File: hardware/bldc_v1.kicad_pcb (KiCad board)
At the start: 4 copper layers, 63 parts, among them J1 Conn_01x06, J2 1x2_ScrewTerminal_65A, J3 Screw_Terminal_01x05, J4 RJ45, J5 Screw_Terminal_01x03, M1 IPB044N15N5, M2 IPB044N15N5, M3 IPB044N15N5, M4 IPB044N15N5, M5 IPB044N15N5, M6 IPB044N15N5, M7 STM32F4-DISCOVERY, U1 AD8205, U2 AD8205

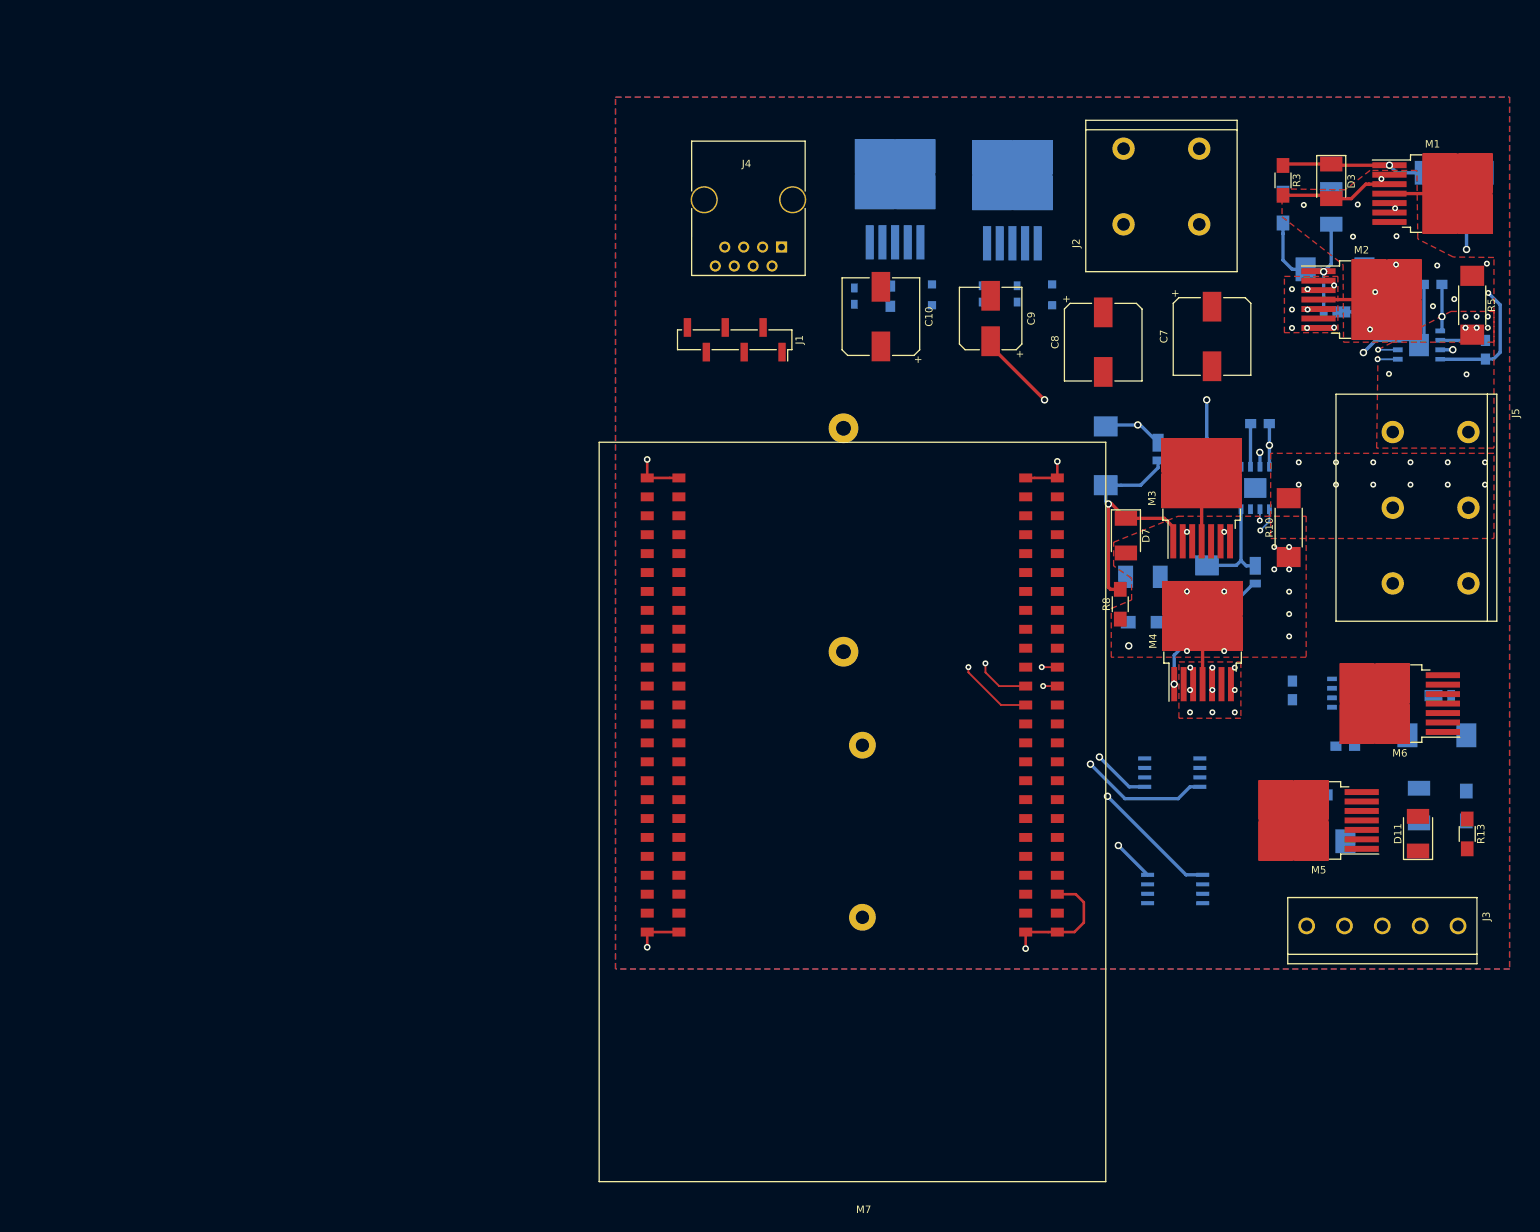
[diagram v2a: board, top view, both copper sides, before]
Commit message: Completed routing
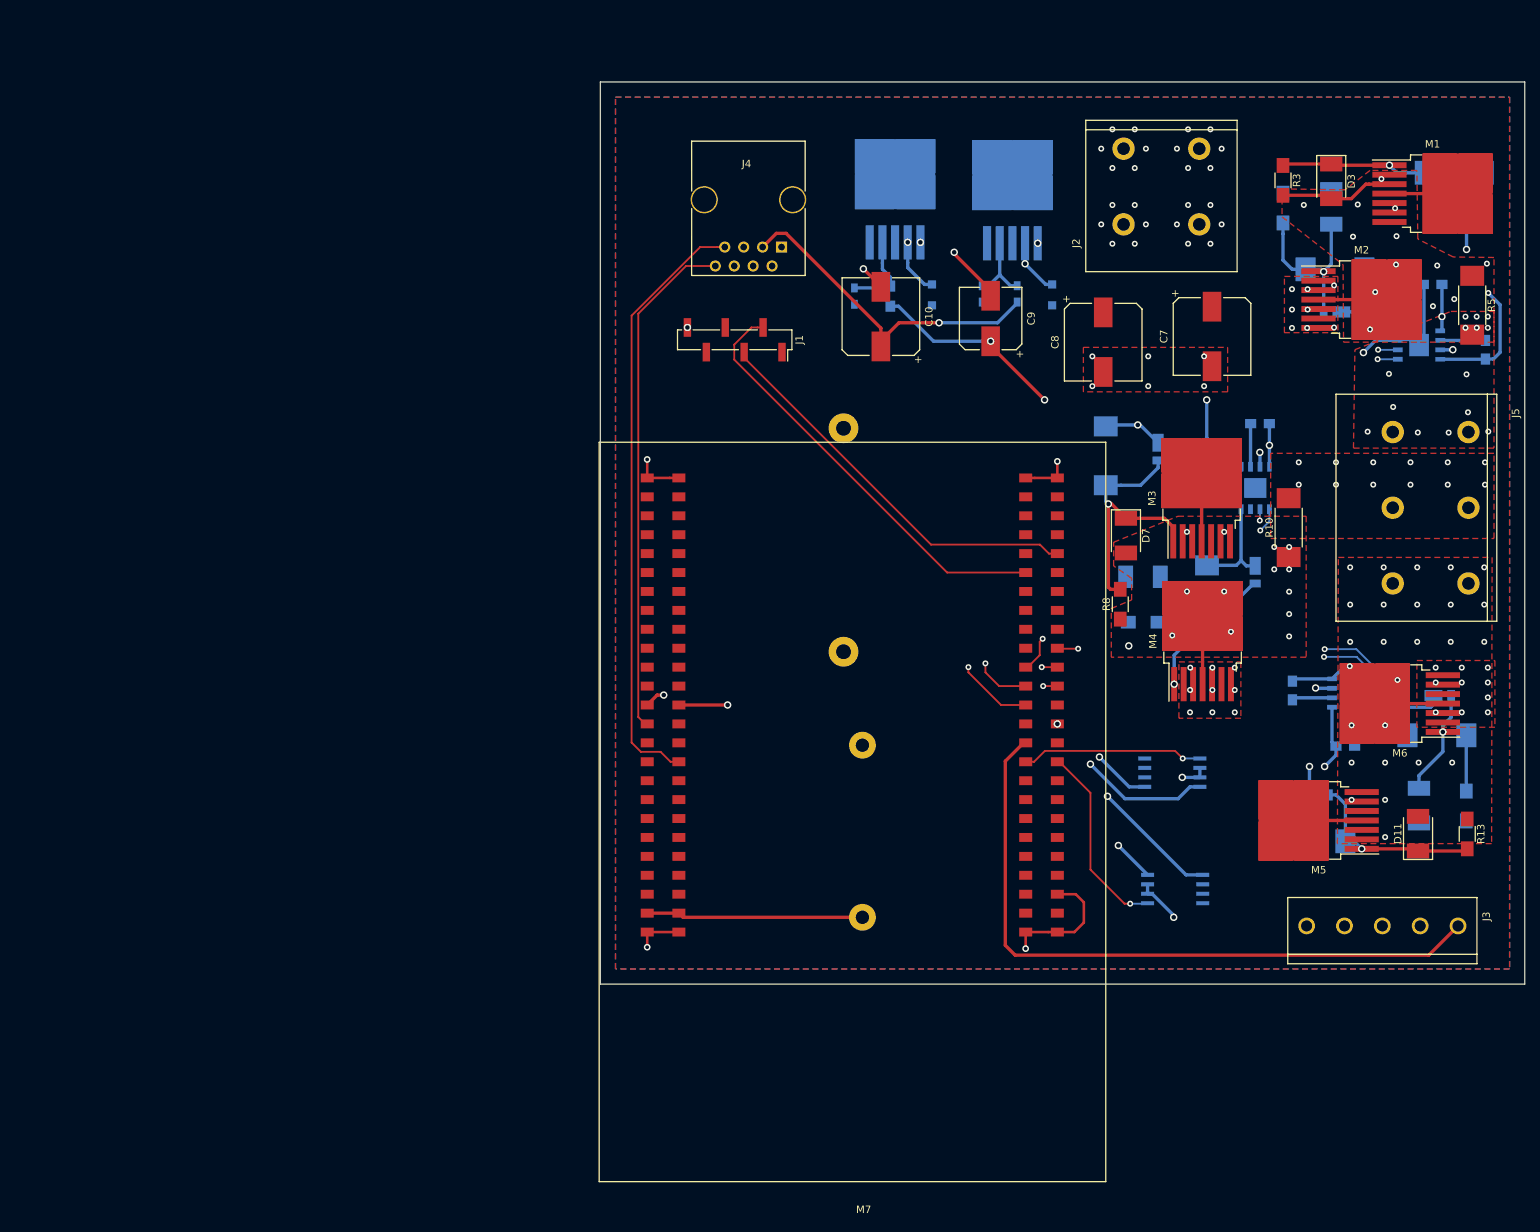
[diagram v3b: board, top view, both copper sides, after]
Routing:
- net /5v: track 0.00 -> 248.1 mm, vias 0 -> 3
- net /GateDriver/+12V: track 90.4 -> 236.9 mm, vias 3 -> 5
- net /Microcontroller/HALL_B: track 0.00 -> 118.4 mm, vias 0 -> 1
- net /Microcontroller/HALL_A: track 0.00 -> 108.0 mm, vias 0 -> 1
- net /Microcontroller/HALL_C: track 0.00 -> 91.4 mm
- net Net-(5vConverter1-Pad2): track 0.00 -> 87.1 mm, vias 0 -> 1
- net /Microcontroller/I2C_SCL: track 0.00 -> 81.0 mm
- net /Microcontroller/I2C_SDA: track 0.00 -> 68.7 mm
- net /Microcontroller/USART_TX: track 0.00 -> 57.8 mm
- net /GateDriver/LS_C_TTL_PWM: track 0.00 -> 55.6 mm, vias 0 -> 2
- net /Microcontroller/USART_RX: track 0.00 -> 53.7 mm
- net /GateDriver/HS_C_TTL_PWM: track 0.00 -> 44.6 mm, vias 0 -> 2
- net Net-(12vConverter1-Pad2): track 0.00 -> 36.1 mm, vias 0 -> 1
- net /FB_B: track 0.00 -> 26.1 mm, vias 0 -> 1
- net Net-(D10-Pad2): track 0.00 -> 25.1 mm, vias 0 -> 1
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- added copper zone on Inner2.Cu, net /48v
- added copper zone on Inner3.Cu, net /48v
- added copper zone on Inner2.Cu, net /GND
- added copper zone on Inner3.Cu, net /GND
- added copper zone on F.Cu, net /MOSFETS/PhaseC
- added copper zone on Inner2.Cu, net /MOSFETS/PhaseC
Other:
- board outline added: 124.1 x 121.1 mm

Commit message: Added additional planes for extra current
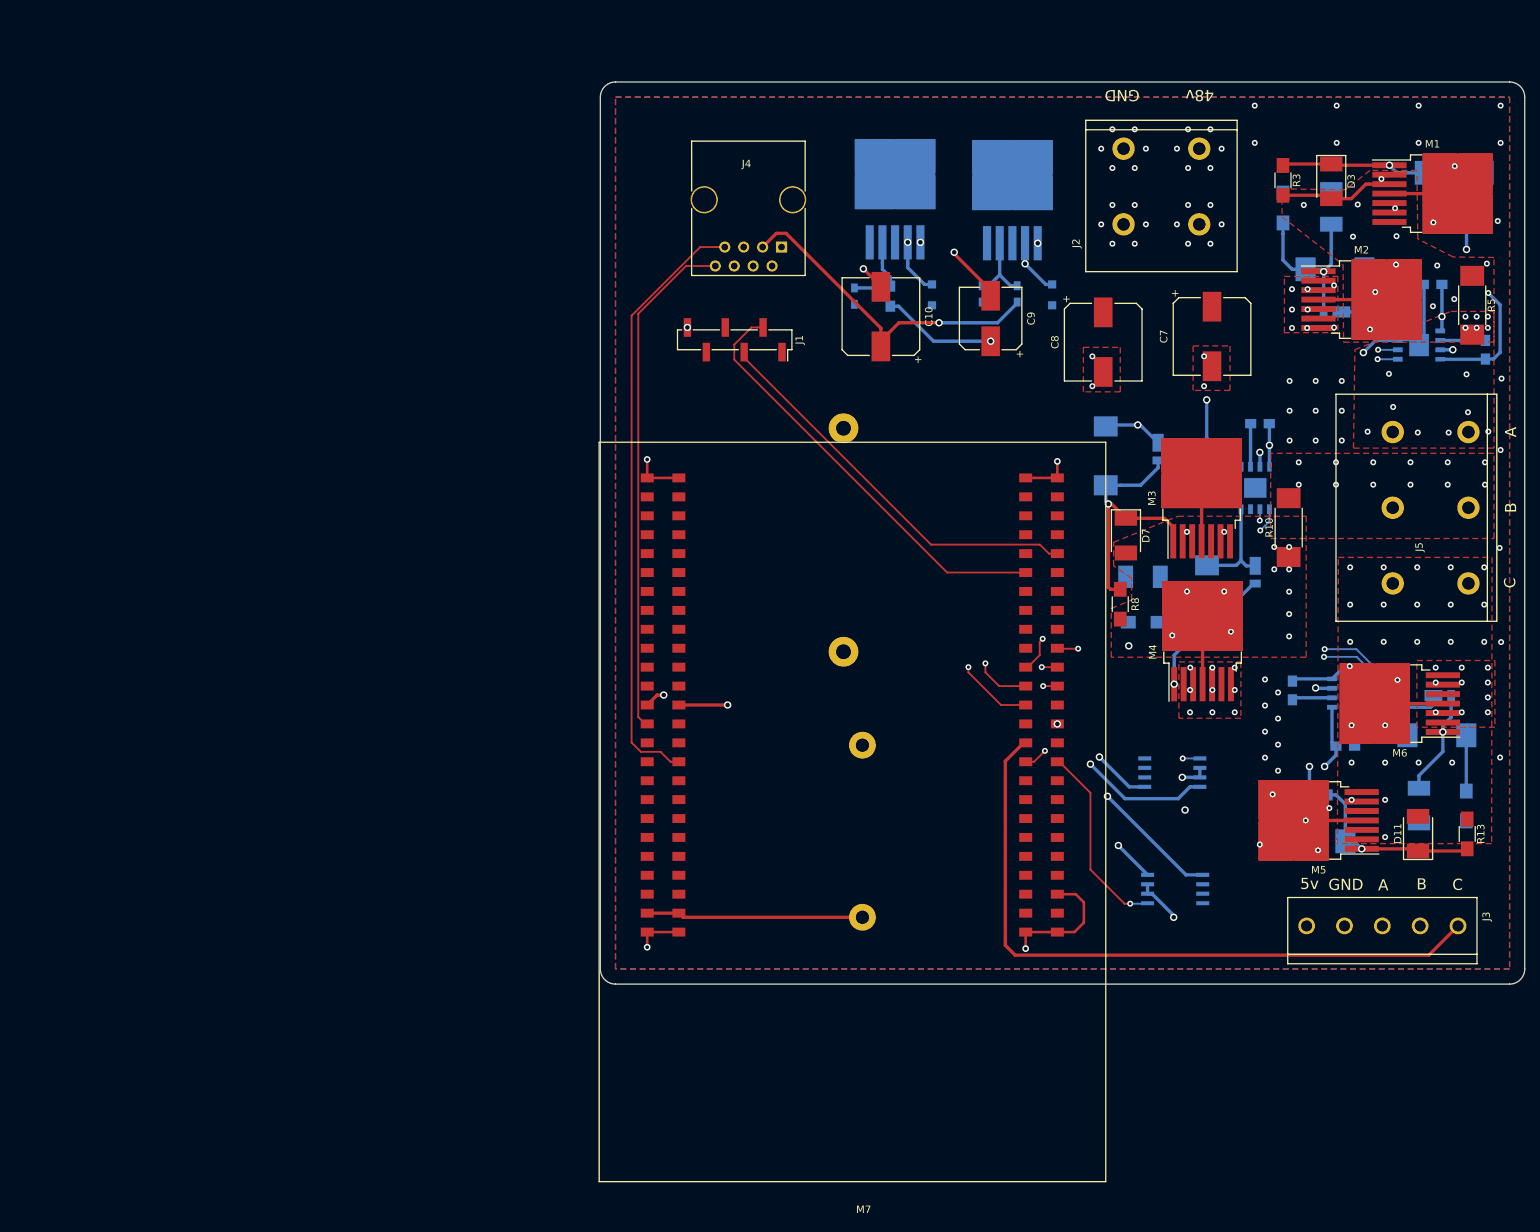
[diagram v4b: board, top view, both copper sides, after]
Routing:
- net /FB_A: vias 1 -> 2
- net /48v: vias 14 -> 50
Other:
- outline, holes or cut-outs redrawn
- board text added: "48v"
- board text added: "5v"
- board text added: "A"
- board text added: "B"
- board text added: "C"
- board text added: "GND"

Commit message: updated routing and all plots
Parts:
- moved 12vConverter1 36.4 mm to (117.5, 38.8)
- moved 5vConverter1 36.4 mm to (133.3, 38.9)
- moved C1 36.4 mm to (166.5, 68.9)
- moved C10 36.4 mm to (115.6, 54.5)
- moved C2 36.4 mm to (170.9, 104.7)
- moved C3 36.4 mm to (196.8, 59.0)
- moved C4 36.4 mm to (189.7, 50.2)
- moved C5 36.4 mm to (158.8, 75.7)
- moved C6 36.4 mm to (178.0, 112.2)
- moved C7 36.4 mm to (160.1, 57.2)
- moved C8 36.4 mm to (145.5, 58.0)
- moved C9 36.4 mm to (130.4, 54.8)
- moved D1 36.4 mm to (192.8, 40.1)
- moved D10 36.4 mm to (190.7, 105.4)
- moved D11 36.4 mm to (187.7, 124.0)
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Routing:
- net /48v: track 27.4 -> 82.2 mm
- net /GND: track 63.0 -> 106.9 mm, vias 54 -> 66
- net /GateDriver/PhaseASource: track 145.9 -> 130.7 mm
- net /GateDriver/+12V: track 236.7 -> 237.8 mm
- net /MOSFETS/PhaseC: vias 26 -> 27
- net /MOSFETS/PhaseB: vias 13 -> 17
- net /GateDriver/PhaseBSource: vias 16 -> 17

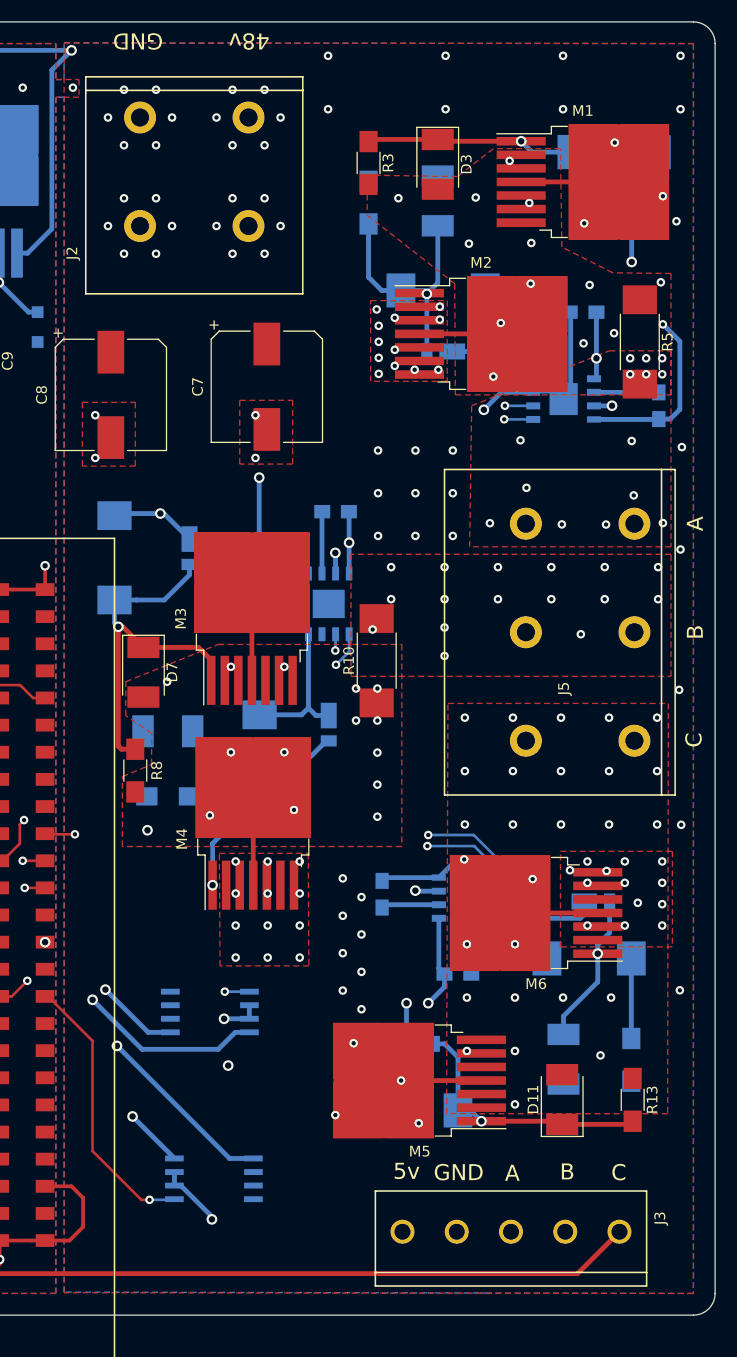
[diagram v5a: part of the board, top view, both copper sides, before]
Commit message: Updated schematic for additional capacitors
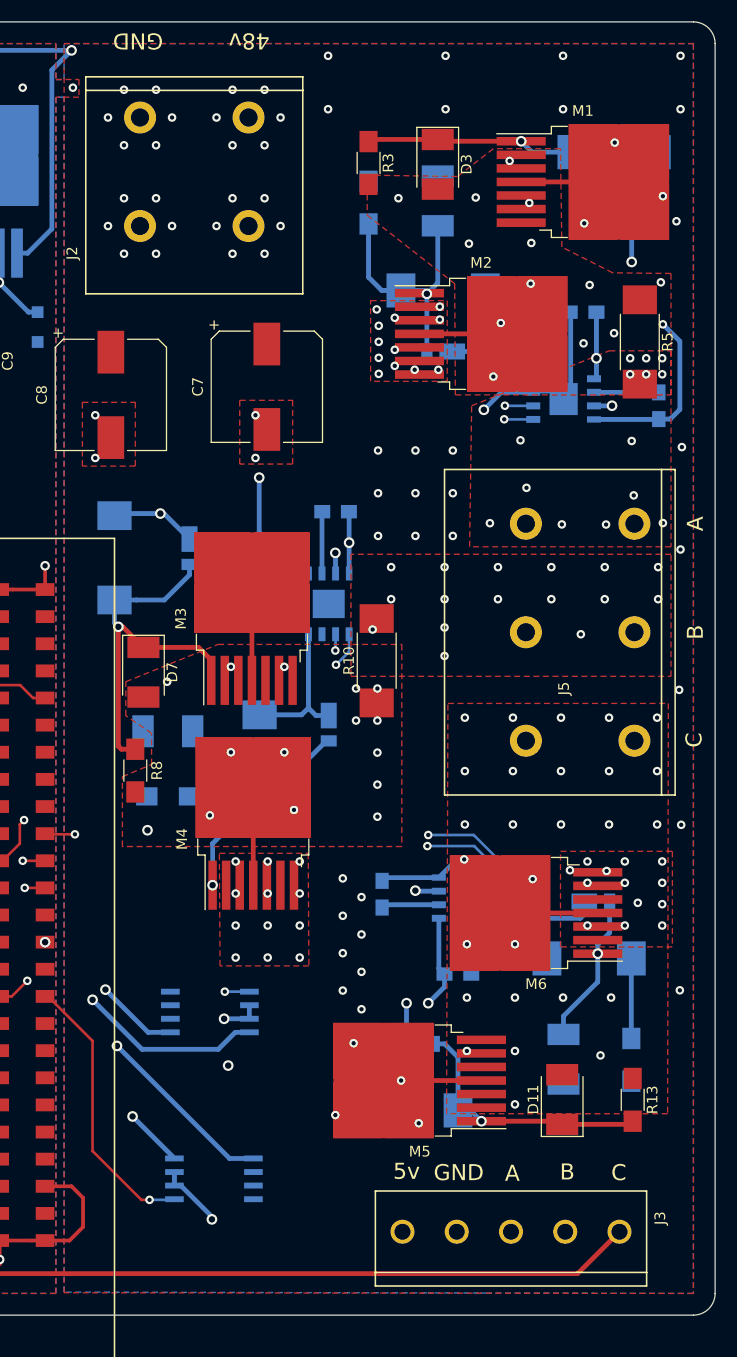
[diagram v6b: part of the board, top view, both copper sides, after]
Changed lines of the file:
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@@
   (general
     (thickness 1.6)
-    (drawings 20)
+    (drawings 18)
     (tracks 666)
     (zones 0)
@@
       (net 1 /GND))
   )
-  (dimension 121.0945 (width 0.3) (layer Eco1.User)
-    (gr_text "121.094 mm" (at 99.4365 92.55125 270) (layer Eco1.User)
-      (effects (font (size 1.5 1.5) (thickness 0.3)))
-    )
-    (feature1 (pts (xy 113.2205 153.0985) (xy 100.950079 153.0985)))
-    (feature2 (pts (xy 113.2205 32.004) (xy 100.950079 32.004)))
-    (crossbar (pts (xy 101.5365 32.004) (xy 101.5365 153.0985)))
-    (arrow1a (pts (xy 101.5365 153.0985) (xy 100.950079 151.971996)))
-    (arrow1b (pts (xy 101.5365 153.0985) (xy 102.122921 151.971996)))
-    (arrow2a (pts (xy 101.5365 32.004) (xy 100.950079 33.130504)))
-    (arrow2b (pts (xy 101.5365 32.004) (xy 102.122921 33.130504)))
-  )
-  (dimension 124.079 (width 0.3) (layer Eco1.User)
-    (gr_text "124.079 mm" (at 175.26 163.1995) (layer Eco1.User)
-      (effects (font (size 1.5 1.5) (thickness 0.3)))
-    )
-    (feature1 (pts (xy 113.2205 153.0985) (xy 113.2205 161.685921)))
-    (feature2 (pts (xy 237.2995 153.0985) (xy 237.2995 161.685921)))
-    (crossbar (pts (xy 237.2995 161.0995) (xy 113.2205 161.0995)))
-    (arrow1a (pts (xy 113.2205 161.0995) (xy 114.347004 160.513079)))
-    (arrow1b (pts (xy 113.2205 161.0995) (xy 114.347004 161.685921)))
-    (arrow2a (pts (xy 237.2995 161.0995) (xy 236.172996 160.513079)))
-    (arrow2b (pts (xy 237.2995 161.0995) (xy 236.172996 161.685921)))
-  )
   (gr_text GND (at 148.0185 24.8285 180) (layer F.SilkS)
     (effects (font (size 1.5 1.5) (thickness 0.3)))
@@
         (xy 175.069616 142.059217) (xy 141.097 141.986) (xy 141.097 30.099) (xy 140.335 30.099) (xy 140.335 142.113)
         (xy 80.01 142.113) (xy 80.01 25.0825) (xy 140.335 25.0825) (xy 140.335 28.448) (xy 141.097 28.448)
-        (xy 141.097 25.019)
+        (xy 141.097 25.0825)
       )
     )
@@
     (polygon
       (pts
-        (xy 200.025 142.113) (xy 141.097 142.0495) (xy 141.097 25.019) (xy 200.025 25.0825)
+        (xy 200.025 142.113) (xy 141.097 142.0495) (xy 141.097 25.0825) (xy 200.025 25.0825)
       )
     )
@@
       (pts
         (xy 200.025 25.0825) (xy 200.088903 44.0055) (xy 188.595 43.8785) (xy 188.595 33.9725) (xy 167.957903 33.9725)
-        (xy 167.957903 35.687) (xy 162.814 35.687) (xy 162.814 46.101) (xy 154.178 46.101) (xy 154.178 28.194)
-        (xy 161.925 28.194) (xy 161.925 25.0825)
+        (xy 167.957903 35.687) (xy 162.814 35.687) (xy 162.814 46.101) (xy 154.178 46.101) (xy 154.178 25.0825)
+        (xy 161.9885 25.0825)
       )
     )
@@
         (xy 200.025 25.0825) (xy 200.025 44.0055) (xy 188.595 43.815) (xy 188.595 33.909) (xy 167.894 33.9725)
         (xy 167.894 35.687) (xy 162.814 35.687) (xy 162.814 46.035527) (xy 154.178 46.035527) (xy 154.178 28.128527)
-        (xy 161.925 28.128527) (xy 161.925 25.0825)
+        (xy 154.178 28.1305) (xy 154.178 25.084473)
       )
     )
@@
     (polygon
       (pts
-        (xy 143.9545 28.2575) (xy 152.654 28.2575) (xy 152.654 46.101) (xy 143.9545 46.101)
+        (xy 144.018 25.0825) (xy 152.654 25.0825) (xy 152.654 46.0375) (xy 144.018 46.0375)
       )
     )
@@
     (polygon
       (pts
-        (xy 143.9545 28.198765) (xy 152.654 28.198765) (xy 152.654 46.042265) (xy 143.9545 46.042265)
+        (xy 144.018 25.077735) (xy 152.7175 25.0825) (xy 152.654 46.042265) (xy 144.018 46.0375)
       )
     )
